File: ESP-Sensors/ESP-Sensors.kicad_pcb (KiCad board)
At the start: 2 copper layers, 19 parts, among them J1 PROG_CONN, J2 GPIO, J3 CONN_01X05, J4 +5V GND +3.3V, SW1 SW_Push, SW2 SW_Push, U1 ESP-12E

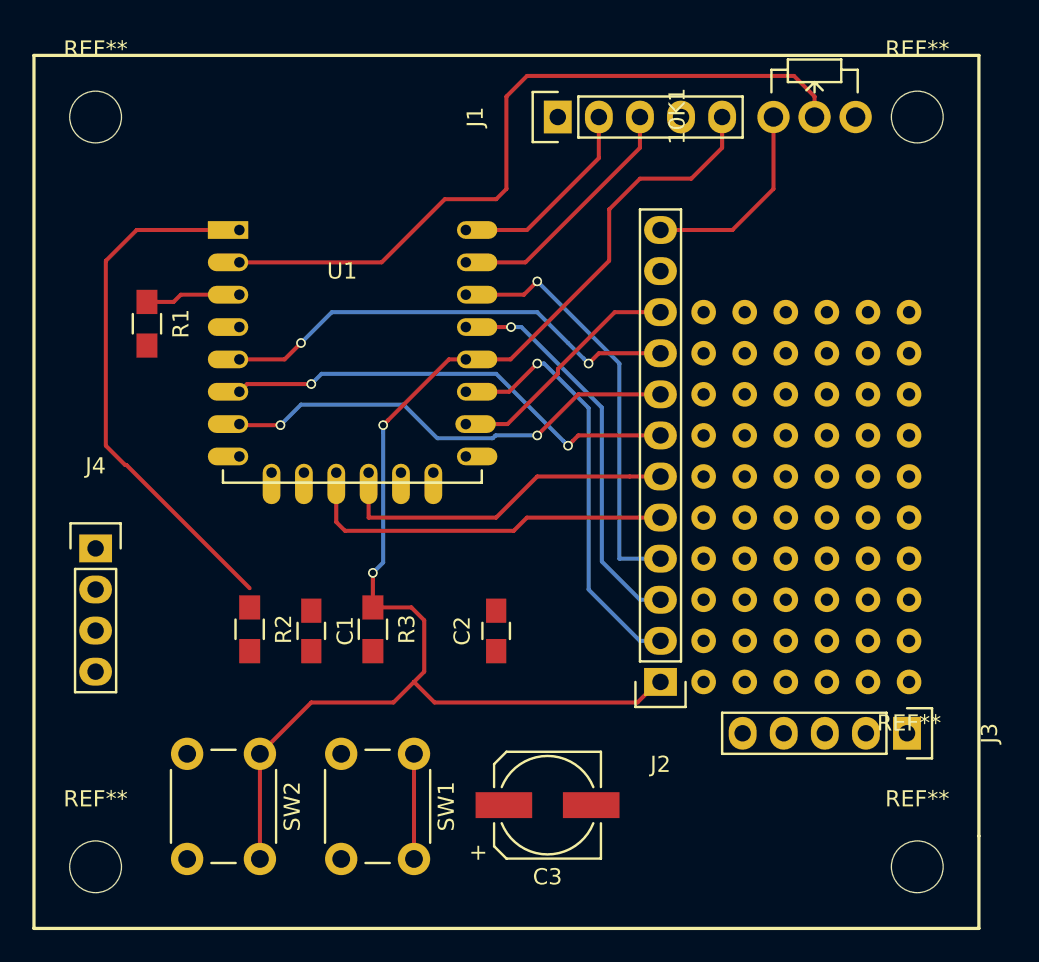
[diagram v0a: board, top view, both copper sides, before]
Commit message: fixed U2 power connection, more traces
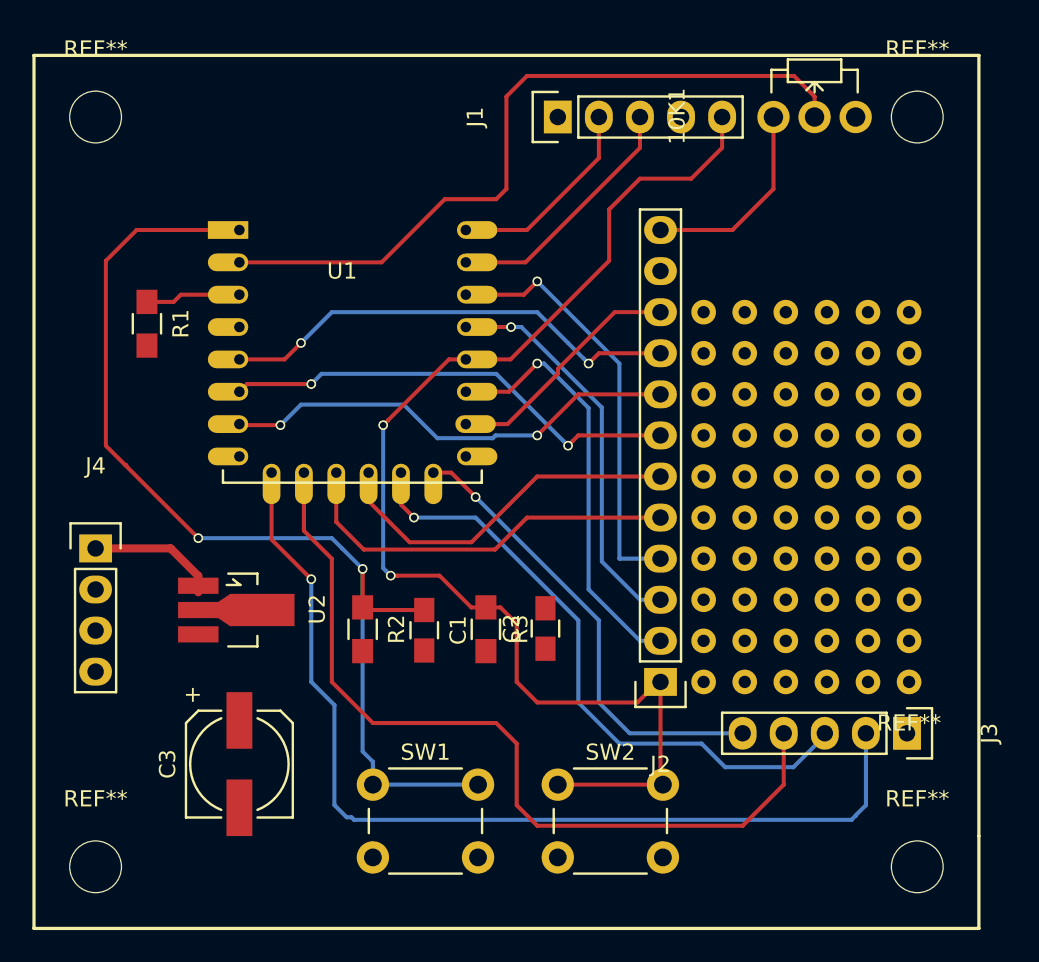
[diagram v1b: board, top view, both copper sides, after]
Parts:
- added U2: HT7333, TO_SOT_Packages_SMD:SOT89-3_Housing_Handsoldering, F.Cu at (119.8, 95.9)
- J4: value +5V GND +3.3V -> +3.3V GND +5V
- moved C3 19.2 mm to (120.0, 105.4), turned to 270 degrees
- moved SW2 18.5 mm to (139.7, 106.7), turned to 0 degrees
- moved C1 6.99 mm to (131.4, 97.1)
- moved R2 6.98 mm to (127.6, 97.1)
- moved R3 6.98 mm to (135.3, 97.1)
- moved SW1 3.17 mm to (128.3, 106.7), turned to 0 degrees
- moved C2 3.05 mm to (138.9, 97.0)
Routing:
- net /CS0: track 0.00 -> 60.2 mm, vias 0 -> 1
- net /MISO: track 0.00 -> 51.7 mm
- net /MOSI: track 0.00 -> 38.8 mm, vias 0 -> 1
- net /SLCK: track 0.00 -> 28.8 mm, vias 0 -> 1
- net Net-(C1-Pad1): track 39.5 -> 65.9 mm, vias 0 -> 2
- net /GPIO0: track 85.1 -> 76.8 mm
- net Net-(J4-Pad1): track 0.00 -> 8.23 mm
- net /GPIO9: track 23.7 -> 24.6 mm
- net /GPIO10: track 21.9 -> 22.5 mm
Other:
- net class Power added: clearance 0.2, trace_width 0.504, via_dia 0.6, via_drill 0.4

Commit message: all traced layed out, DRC, labels correct
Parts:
- added ?: proto_grid_6x10, ESP-RS232:proto_grid_6x10, F.Cu at (153.0, 74.9)
- added J2: GPIO, Pin_Headers:Pin_Header_Straight_1x12, B.Cu at (146.1, 100.3)
- added REF**: GPIO, Pin_Headers:Pin_Header_Straight_1x06, F.Cu at (148.7, 74.9)
- 10K1: value POT -> Analog Trim
- J3: value CONN_01X05 -> SPI
- SW1: value SW_Push -> RESET
- SW2: value SW_Push -> PROG
- moved 10K1 7.10 mm to (156.2, 71.8)
- moved J3 0.13 mm to (161.4, 103.5)
- turned R3 to 90 degrees
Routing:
- net VCC: track 0.00 -> 30.0 mm, vias 0 -> 3
- net Net-(10K1-Pad2): track 45.5 -> 53.1 mm
- net Net-(C1-Pad1): track 65.9 -> 68.6 mm
- net /ANALOG_IN: track 12.5 -> 10.4 mm
- net /GPIO0: track 76.8 -> 77.5 mm
- added copper zone on F.Cu, net GND
- added copper zone on B.Cu, net VCC
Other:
- board outline added: 58.4 x 54 mm
- board text added: "15 14 13 12 10 9 5 4 2 0"

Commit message: re-routed ground + analog
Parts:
- removed the J2 at (146.1, 100.3)
- removed the REF** at (153.0, 74.9)
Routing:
- net Net-(10K1-Pad2): track 53.1 -> 53.3 mm, vias 0 -> 2

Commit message: Created gerbers, checkup
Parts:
- added G***: LOGO, ESP-RS232:LOGO2, F.Cu at (153.7, 110.5)
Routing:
- net /SLCK: track 28.8 -> 31.8 mm
- net /MOSI: track 38.8 -> 41.1 mm
- net Net-(C1-Pad1): track 68.6 -> 69.7 mm
- net Net-(10K1-Pad2): track 53.3 -> 53.0 mm, vias 2 -> 1
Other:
- board text added: "ESP-Sensors rev.1"

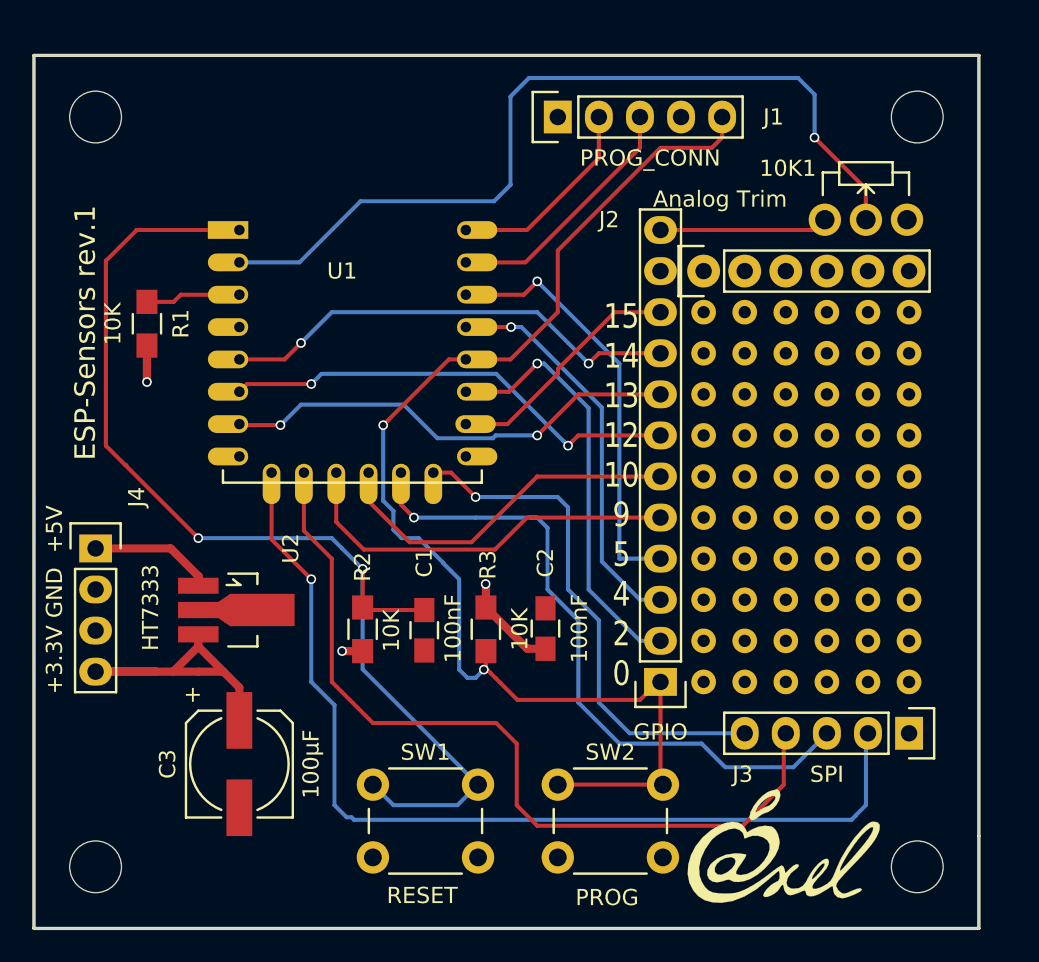
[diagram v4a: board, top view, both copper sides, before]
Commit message: More cleanup of vias
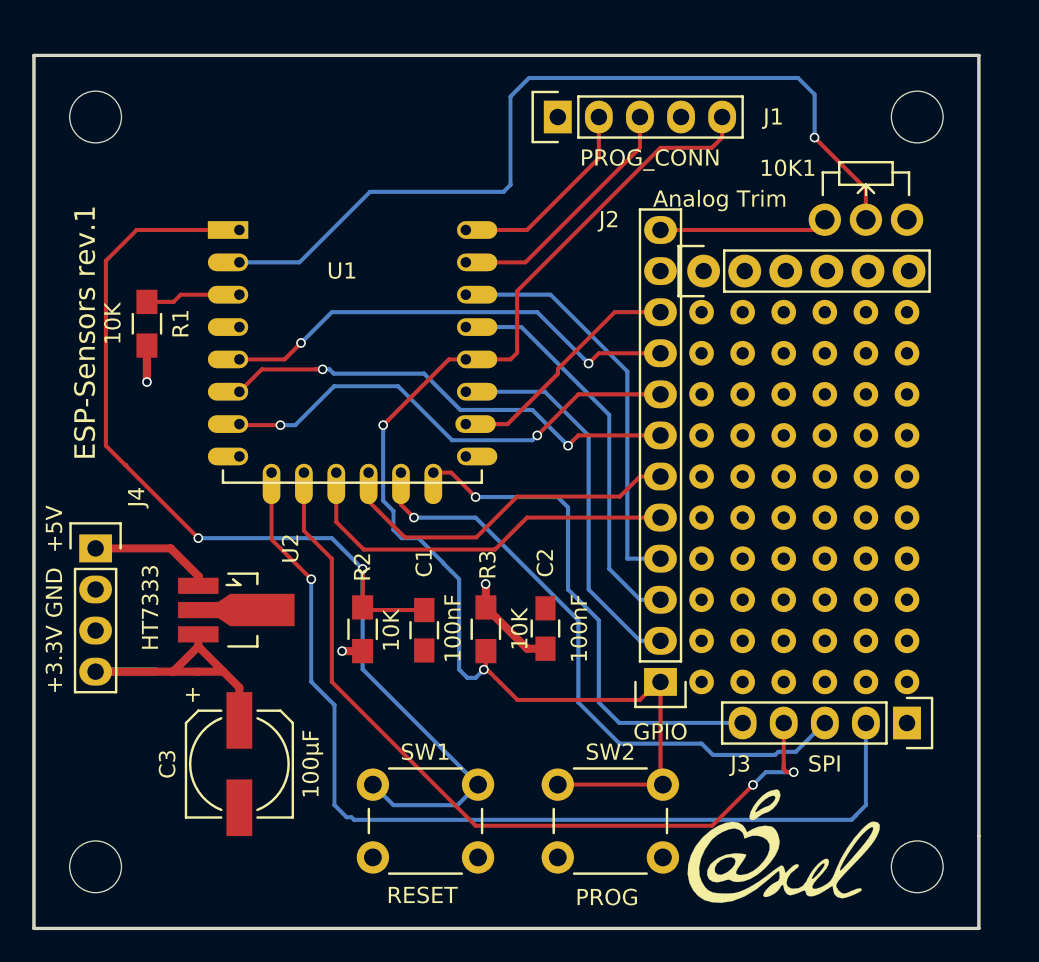
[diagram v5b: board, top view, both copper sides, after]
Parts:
- moved J3 0.65 mm to (161.3, 102.9)
- moved ? 0.13 mm to (152.9, 74.9)
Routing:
- net /MOSI: track 41.1 -> 38.4 mm
- net /GPIO2: track 26.4 -> 24.0 mm, vias 1 -> 0
- net /GPIO13: track 28.6 -> 29.6 mm
- net /GPIO5: track 26.5 -> 25.6 mm, vias 1 -> 0
- net /CS0: track 60.2 -> 60.9 mm
- net /GPIO4: track 24.6 -> 24.9 mm, vias 1 -> 0
- net /MISO: track 51.7 -> 51.9 mm, vias 0 -> 2
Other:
- rule trace_min: 0.2 -> 0.1524
- rule via_min_drill: 0.3 -> 0.3302
- board text removed: "15 14 13 12 10 9 5 4 2 0"

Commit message: added different trimmer plus deep_sleep jumper header
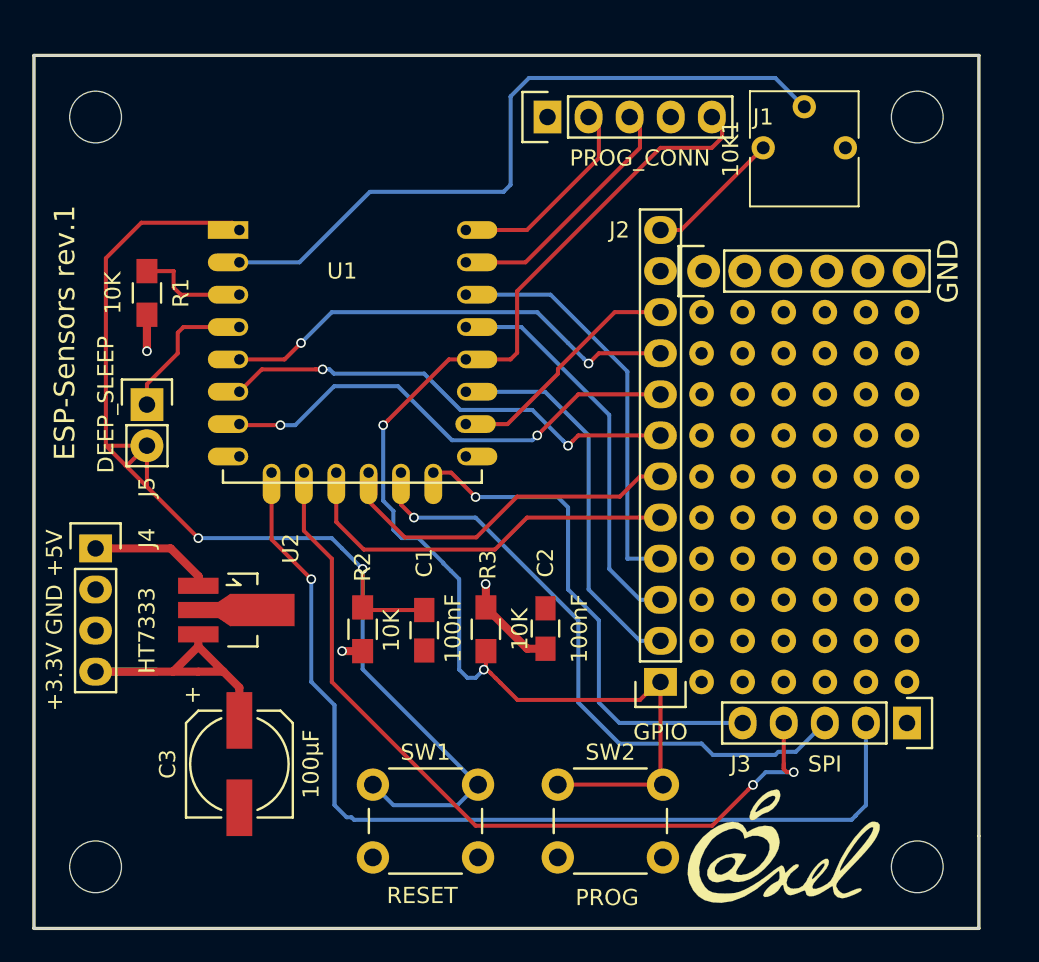
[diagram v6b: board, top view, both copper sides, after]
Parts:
- added J5: DEEP_SLEEP, Pin_Headers:Pin_Header_Straight_1x02, F.Cu at (114.3, 83.2)
- 10K1: value Analog Trim -> POT; footprint Potentiometers:Potentiometer_WirePads_Small -> Potentiometers:Potentiometer_Trimmer_Vishay_T73YP_Horizontal
- J4: value +3.3V GND +5V -> +3.3V GND +5V
- moved 10K1 4.62 mm to (157.5, 67.3)
- moved R1 1.91 mm to (114.3, 76.3)
- moved J1 0.63 mm to (139.1, 65.4)
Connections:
- 10K1 pad 1: /ANALOG_IN -> GND
- 10K1 pad 3: GND -> /ANALOG_IN
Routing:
- net Net-(10K1-Pad2): track 53.0 -> 43.5 mm, vias 1 -> 0
- net Net-(J5-Pad1): track 0.00 -> 9.19 mm
- net Net-(C1-Pad1): track 69.7 -> 77.0 mm
- net /ANALOG_IN: track 10.4 -> 8.45 mm
- net Net-(R1-Pad1): track 5.90 -> 6.91 mm
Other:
- board text added: "GND"

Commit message: Added GPIO refs again and added VCC header
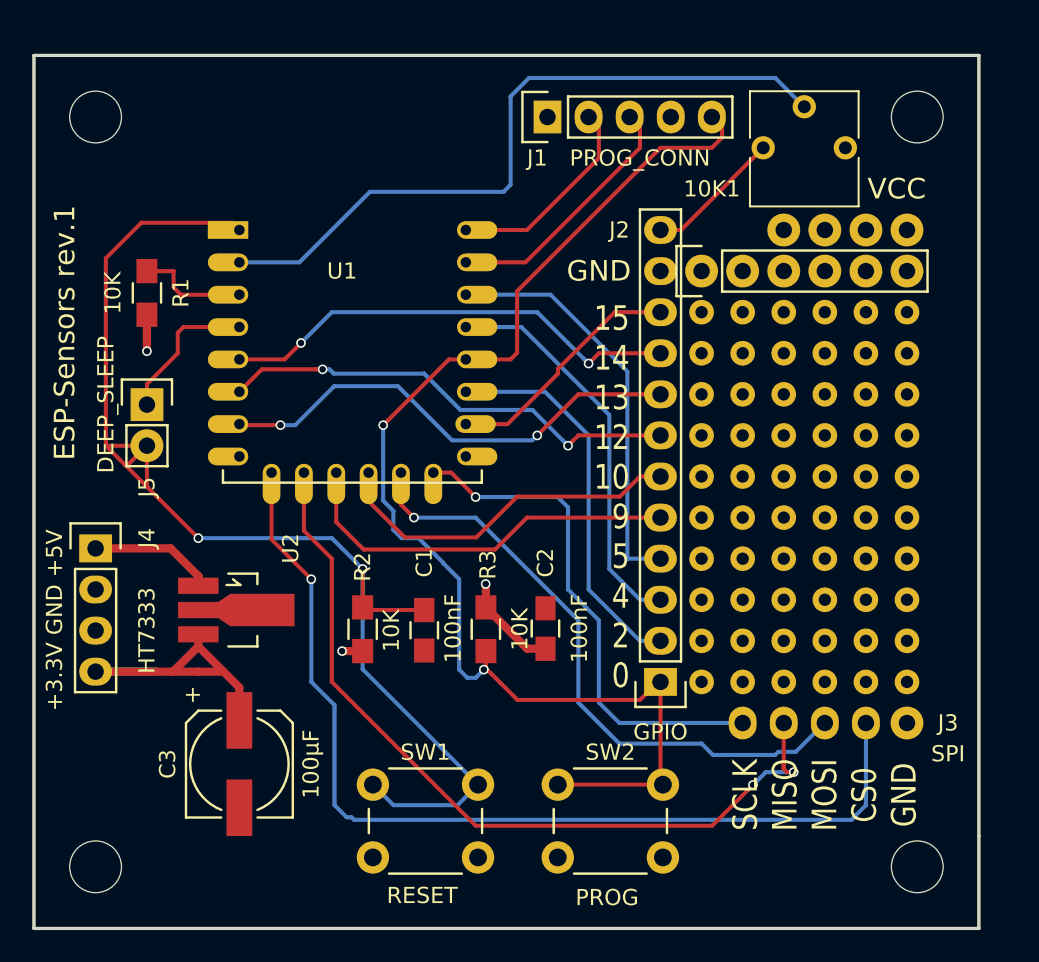
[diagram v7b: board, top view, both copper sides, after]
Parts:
- added REF**: GPIO, Pin_Headers:Pin_Header_Straight_1x06, F.Cu at (148.6, 72.4)
- G***: moved to B.Cu
- J3: footprint Pin_Headers:Pin_Header_Straight_1x05 -> ESP-RS232:SPI_Header
- moved G*** 50.8 mm to (127.0, 67.3), turned to 180 degrees
- moved REF** 0.13 mm to (148.6, 74.9)
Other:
- board text added: "15 14 13 12 10 9 5 4 2 0"
- board text added: "SCLK MISO MOSI CS0 GND"
- board text added: "VCC"
